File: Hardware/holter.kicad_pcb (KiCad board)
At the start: 2 copper layers, 33.5 x 48 mm, 270 parts, among them CN1 2TAP, CN2 2TAP, CN3 3TAP, IC1 256kx8, M1 USB_Power_Module, M2 USB_Power_Module, P1 CONN_01X07, P2 PROG, P3 SCREW, P4 BAT-, Q1 PMF170XP, Q2 PMF170XP, Q3 NTR4101PT1G, Q4 PMF170XP, Q5 PMF170XP, U1 TXB0106, U10 TS5A3159, U11 TS5A3159, U12 ESD_PROTECTOR, U13 ESD_PROTECTOR, U14 ESD_PROTECTOR, U15 ESD_PROTECTOR, U16 ESD_PROTECTOR, U17 ESD_PROTECTOR, U18 ESD_PROTECTOR, U19 ESD_PROTECTOR, U2 TXB0106, U20 ESD_PROTECTOR, U21 ESD_PROTECTOR, U22 ESD_PROTECTOR, U23 ESD_PROTECTOR, U24 TLV61220, U25 TLV61220, U26 TLV61220, U27 LM3671, U28 DS2710, U29 LIS2DH12, U3 TiWi-uB2, U4 STM32F4x1_64, U5 uSD, U6 ADS1298, U7 USBULC6-2M6, U8 USB2641, U9 OPA379, X1 32768, Y1 24 MHz, Y2 10 MHz

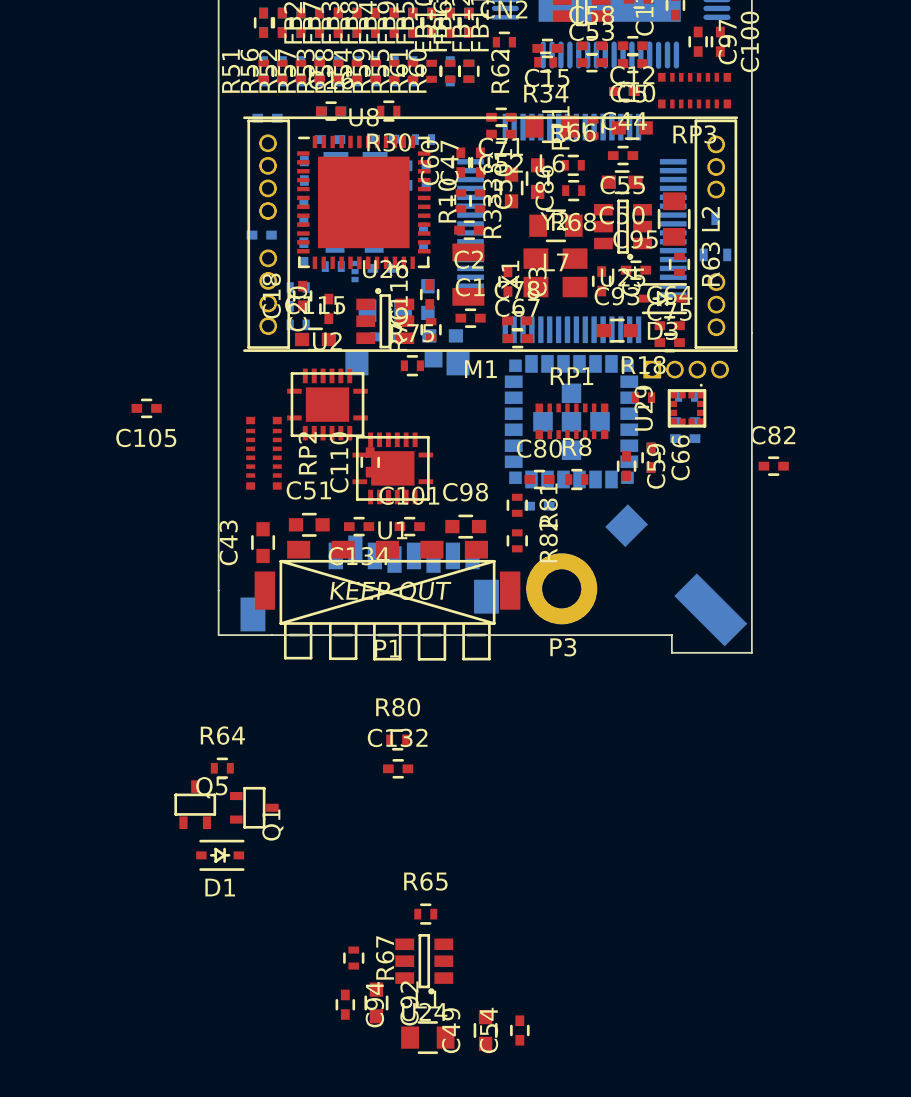
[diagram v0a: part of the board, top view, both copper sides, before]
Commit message: Placement + additional bypass capacitors.
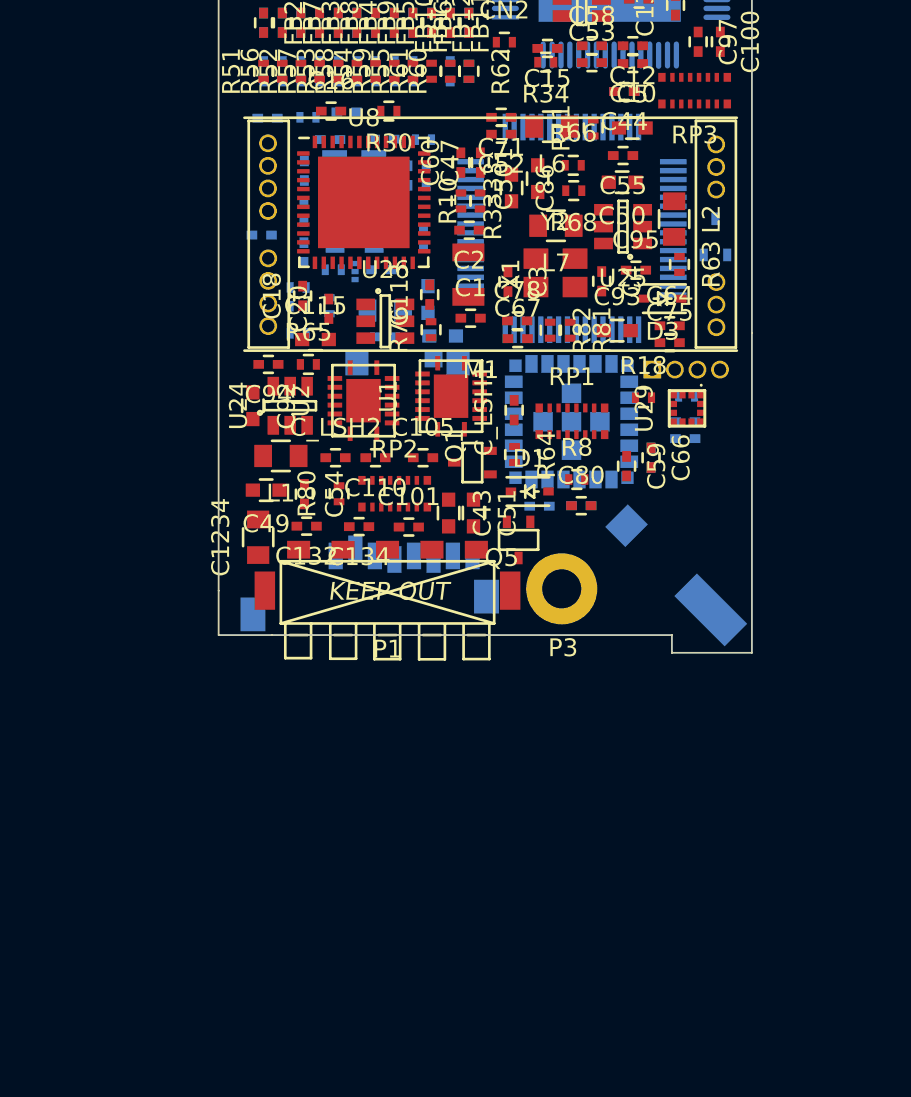
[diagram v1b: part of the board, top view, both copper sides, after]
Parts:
- removed C98: 10uF, Capacitors_SMD:C_0603
- added C1234: 22uF, Capacitors_SMD:C_0805, F.Cu at (77.2, 76.5)
- added C_LSH1: 100nF, Capacitors_SMD:C_0402, F.Cu at (91.6, 69.3)
- added C_LSH2: 100nF, Capacitors_SMD:C_0402, F.Cu at (81.6, 72.0)
- C51: value 10uF -> 22uF
- C82, R67, R75: moved to B.Cu
- moved C94 36.3 mm to (77.8, 66.8), turned to 180 degrees
- moved R67 35.3 mm to (79.5, 65.0), turned to 180 degrees
- moved C92 34.3 mm to (76.9, 69.1)
- moved L1 33.7 mm to (78.5, 71.9), turned to 180 degrees
- moved C49 32.8 mm to (77.7, 73.8), turned to 180 degrees
- moved C54 32.5 mm to (79.8, 74.1), turned to 270 degrees
- moved U24 32.1 mm to (79.0, 69.1), turned to 90 degrees
- moved R65 31.6 mm to (80.0, 66.8)
- moved D1 26.9 mm to (92.5, 73.9), turned to 0 degrees
- moved R64 24.1 mm to (91.7, 71.8), turned to 270 degrees
- moved Q5 23.5 mm to (91.9, 76.7), turned to 180 degrees
- moved Q1 23.0 mm to (89.3, 72.3), turned to 90 degrees
- moved C105 15.8 mm to (86.5, 72.0), turned to 0 degrees
- moved C132 14.6 mm to (80.0, 75.9), turned to 180 degrees
- moved R80 14.2 mm to (81.8, 74.0), turned to 90 degrees
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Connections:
- U1 pad 1: SDIO_D0 -> SDIO_CLK
- U1 pad 10: Net-(RP2-Pad6) -> Net-(RP2-Pad1)
- U1 pad 11: Net-(RP2-Pad5) -> Net-(RP2-Pad2)
- U1 pad 12: Net-(RP2-Pad4) -> Net-(RP2-Pad3)
- U1 pad 13: Net-(RP2-Pad3) -> Net-(RP2-Pad4)
- U1 pad 14: Net-(RP2-Pad2) -> Net-(RP2-Pad5)
- U1 pad 16: Net-(RP2-Pad1) -> Net-(RP2-Pad6)
- U1 pad 3: SDIO_D1 -> SDIO_CMD
- U1 pad 4: SDIO_D2 -> SDIO_D3
- U1 pad 5: SDIO_D3 -> SDIO_D2
- U1 pad 6: SDIO_CMD -> SDIO_D1
- U1 pad 7: SDIO_CLK -> SDIO_D0

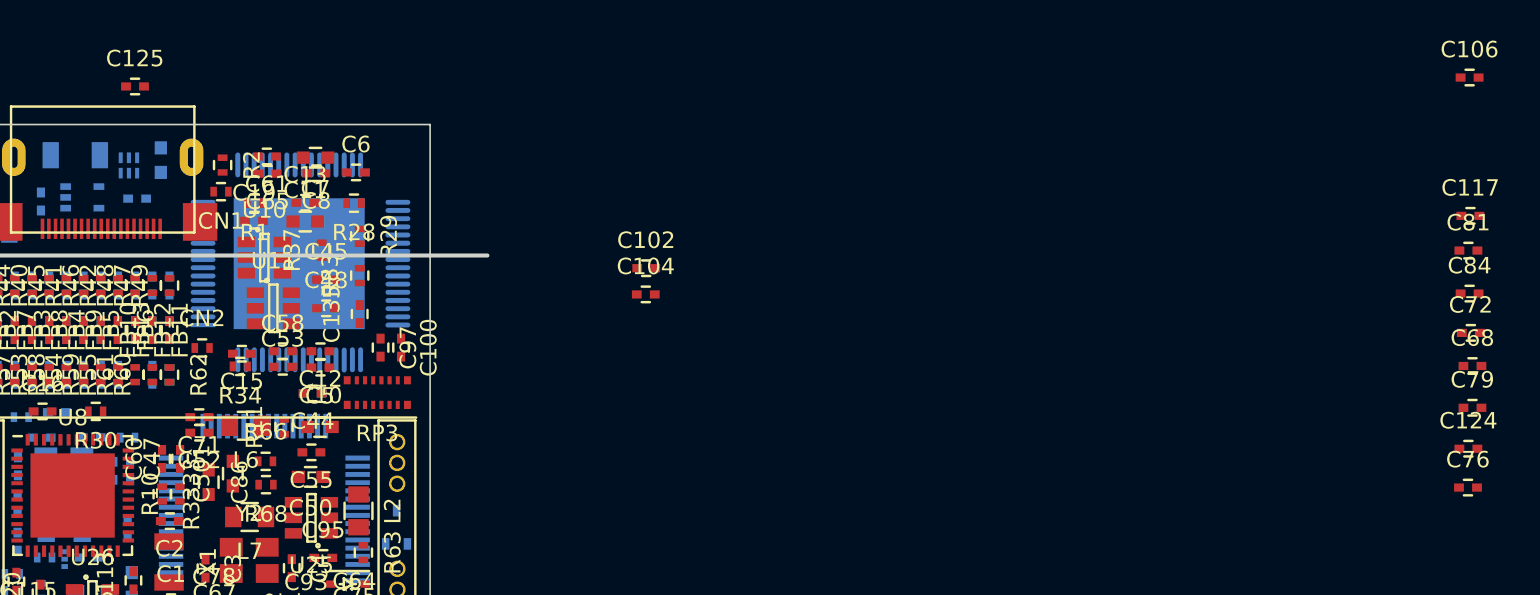
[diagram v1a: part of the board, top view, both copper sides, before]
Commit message: Removed unnecessary bypass capacitors.
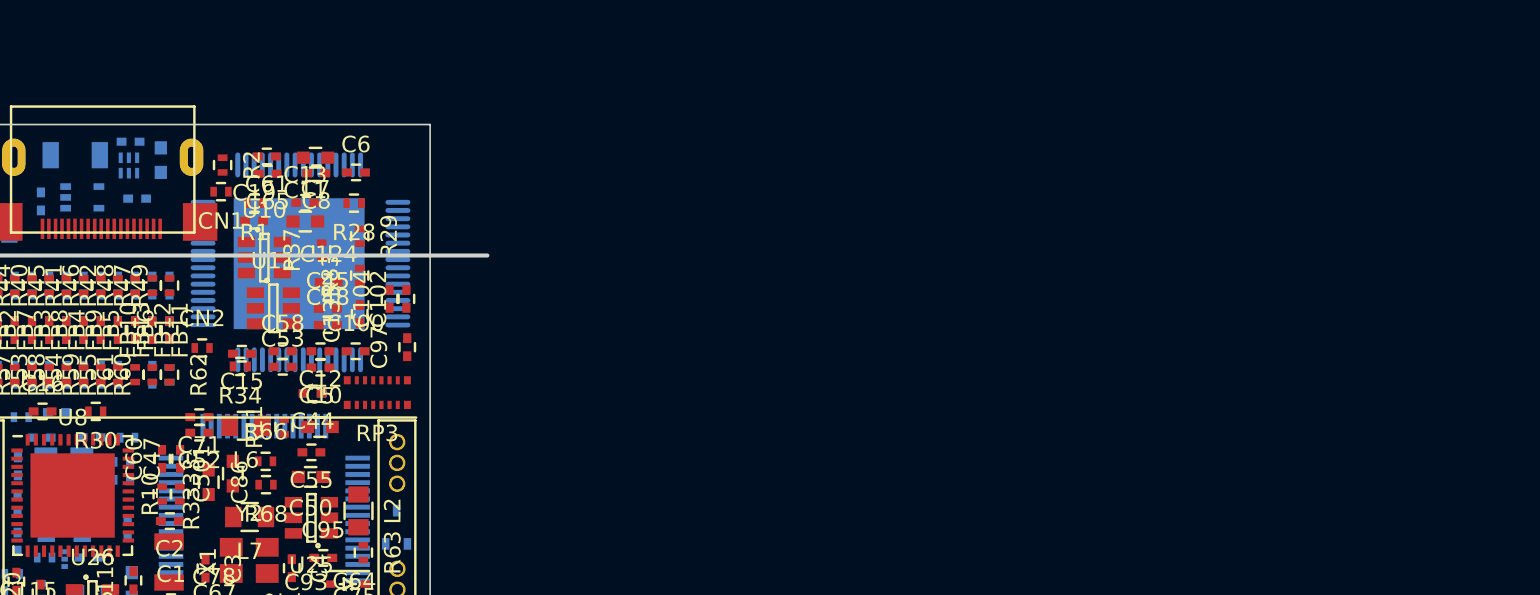
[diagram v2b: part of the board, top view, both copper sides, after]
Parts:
- removed C106, C68, C76, C81: 1uF, Capacitors_SMD:C_0402
- removed C117, C72, C79, C84: 100nF, Capacitors_SMD:C_0402
- C125: moved to B.Cu
- moved C124 70.4 mm to (98.8, 44.6)
- moved C104 15.7 mm to (102.5, 45.6), turned to 90 degrees
- moved C102 14.8 mm to (103.5, 45.6), turned to 90 degrees
- moved C125 3.39 mm to (86.7, 36.0), turned to 180 degrees
- moved C100 2.78 mm to (100.5, 48.9), turned to 0 degrees
- moved C45 1.78 mm to (98.8, 46.2)
- moved C97 1.63 mm to (103.6, 48.6), turned to 90 degrees
- moved C48 1.03 mm to (98.8, 47.2)

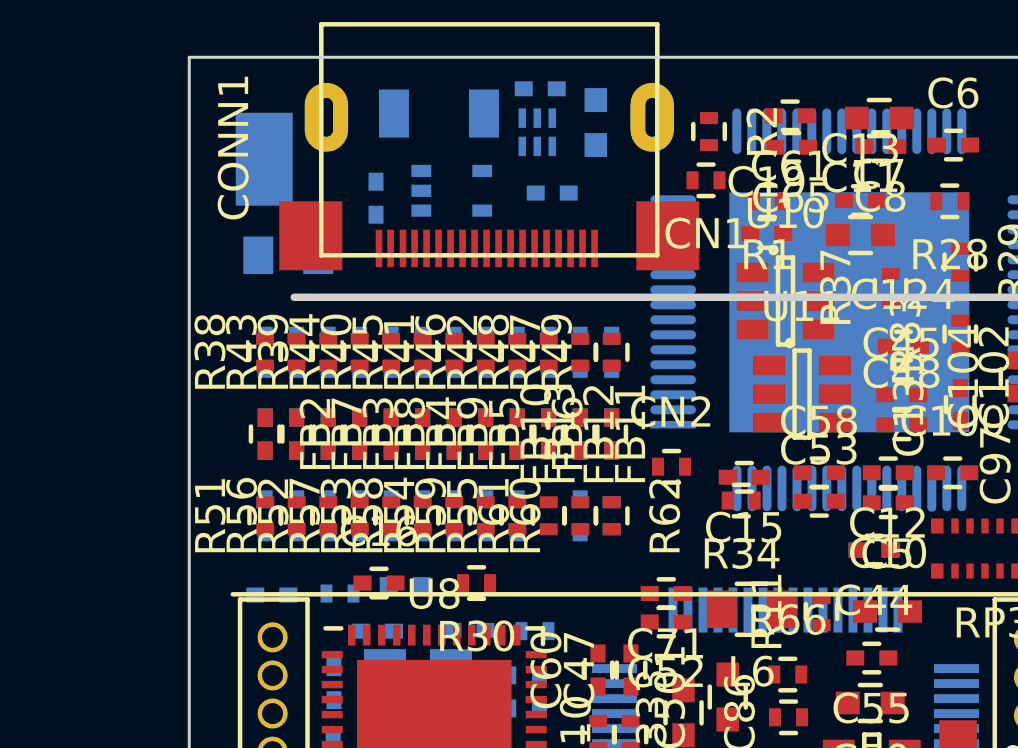
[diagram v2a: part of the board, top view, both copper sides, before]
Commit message: I/O filter connections on PCB.
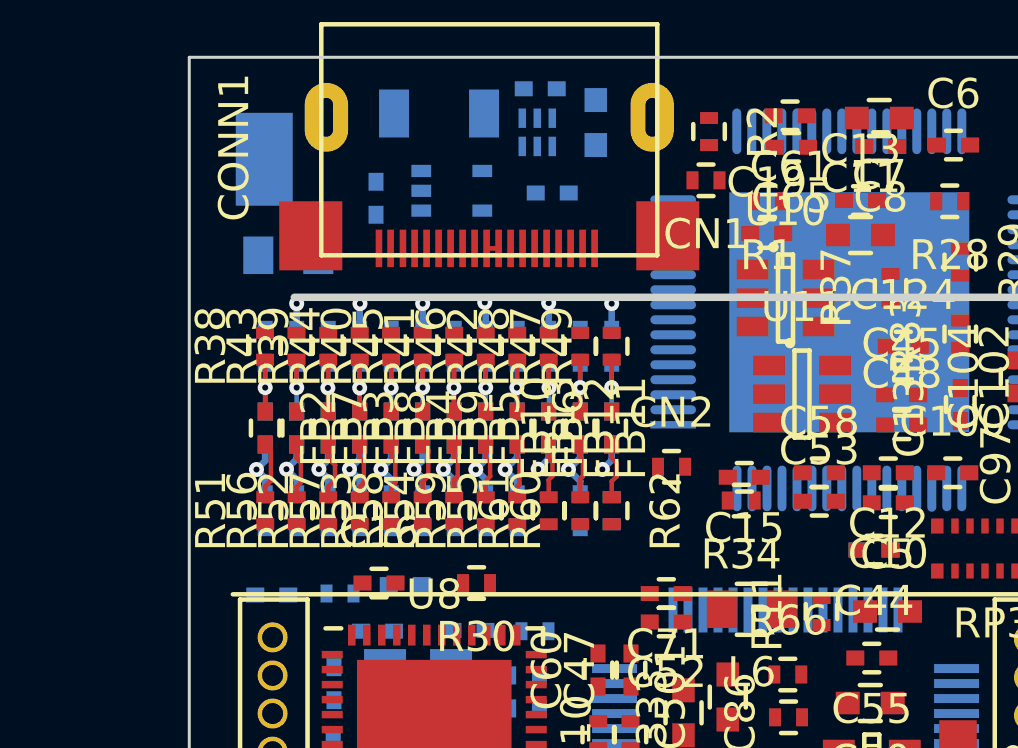
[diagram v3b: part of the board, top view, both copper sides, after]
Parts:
- moved C21 0.20 mm to (89.1, 47.4)
- moved C22 0.20 mm to (77.5, 47.4)
- moved C23 0.20 mm to (79.6, 47.4)
- moved C24 0.20 mm to (81.7, 47.4)
- moved C25 0.20 mm to (83.8, 47.4)
- moved C26 0.20 mm to (85.9, 47.4)
- moved C27 0.20 mm to (78.6, 47.4)
- moved C28 0.20 mm to (80.7, 47.4)
- moved C29 0.20 mm to (82.8, 47.4)
- moved C30 0.20 mm to (84.9, 47.4)
- moved C31 0.20 mm to (88.0, 47.4)
- moved C32 0.20 mm to (87.0, 47.4)
- moved FB10 0.20 mm to (84.9, 47.4)
- moved FB11 0.20 mm to (88.0, 47.4)
- moved FB12 0.20 mm to (87.0, 47.4)
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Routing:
- net GND: track 0.00 -> 26.6 mm, vias 0 -> 18
- net Net-(C26-Pad1): track 0.00 -> 3.37 mm, vias 0 -> 1
- net Net-(C25-Pad1): track 0.00 -> 3.37 mm, vias 0 -> 1
- net Net-(C23-Pad1): track 0.00 -> 3.37 mm, vias 0 -> 1
- net Net-(C22-Pad1): track 0.00 -> 3.35 mm, vias 0 -> 1
- net Net-(C31-Pad1): track 0.00 -> 3.35 mm, vias 0 -> 1
- net Net-(C28-Pad1): track 0.00 -> 3.35 mm, vias 0 -> 1
- net Net-(C32-Pad1): track 0.00 -> 2.56 mm, vias 0 -> 1
- net Net-(C24-Pad1): track 0.00 -> 2.56 mm, vias 0 -> 1
- net Net-(C27-Pad1): track 0.00 -> 2.55 mm, vias 0 -> 1
- net Net-(C30-Pad1): track 0.00 -> 2.55 mm, vias 0 -> 1
- net Net-(C29-Pad1): track 0.00 -> 2.55 mm, vias 0 -> 1
- net Net-(C21-Pad1): track 0.00 -> 2.55 mm, vias 0 -> 1
- net Net-(FB3-Pad2): track 0.00 -> 1.95 mm
- net Net-(FB9-Pad2): track 0.00 -> 1.91 mm
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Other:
- copper layers 2 -> 6
- net class Default: clearance 0.15 -> 0.1524; trace_width 0.15 -> 0.1524; via_dia 0.4 -> 0.5; via_drill 0.15 -> 0.2
- net class High Current added: clearance 0.1524, trace_width 1.5, via_dia 0.7, via_drill 0.4
- net class Power added: clearance 0.1524, trace_width 0.22, via_dia 0.5, via_drill 0.2
- rule trace_clearance: 0.15 -> 0.1524

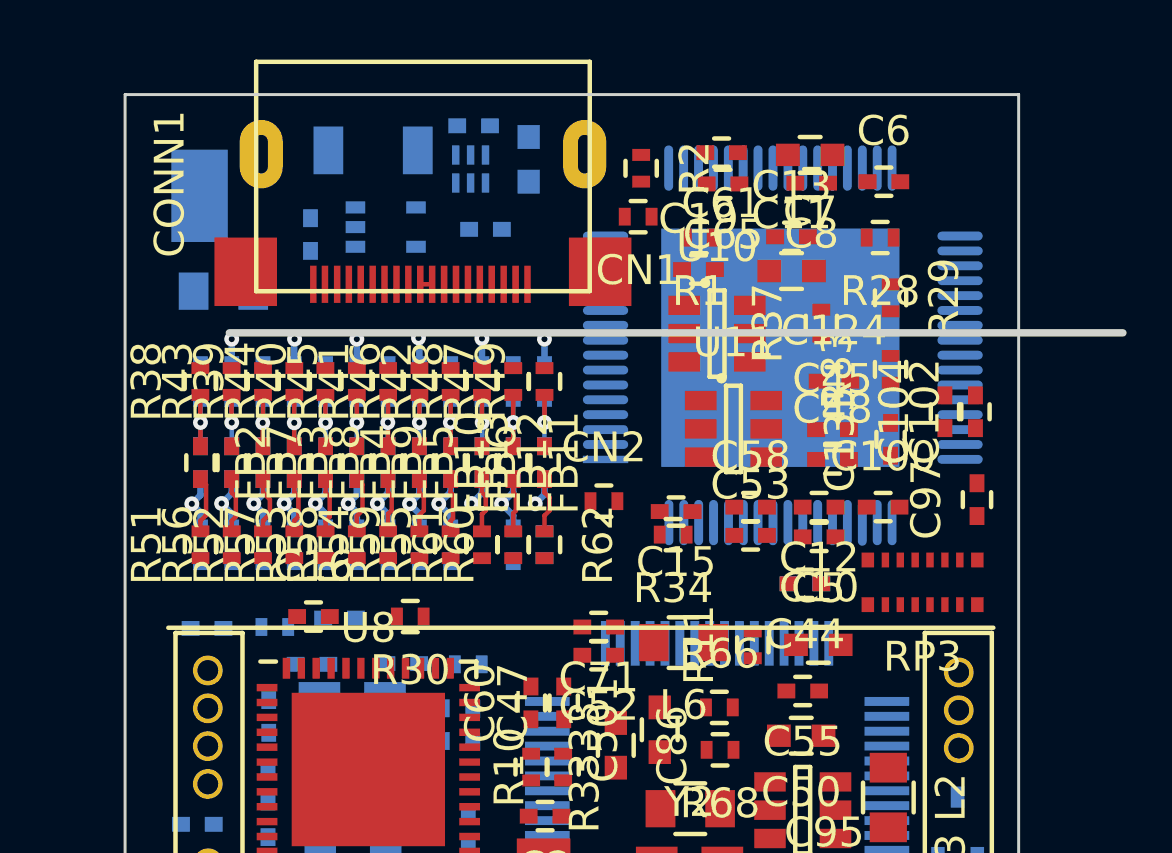
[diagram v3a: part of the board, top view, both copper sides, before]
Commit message: Fixed ADS1298 footprint. Routing of the analog parts.
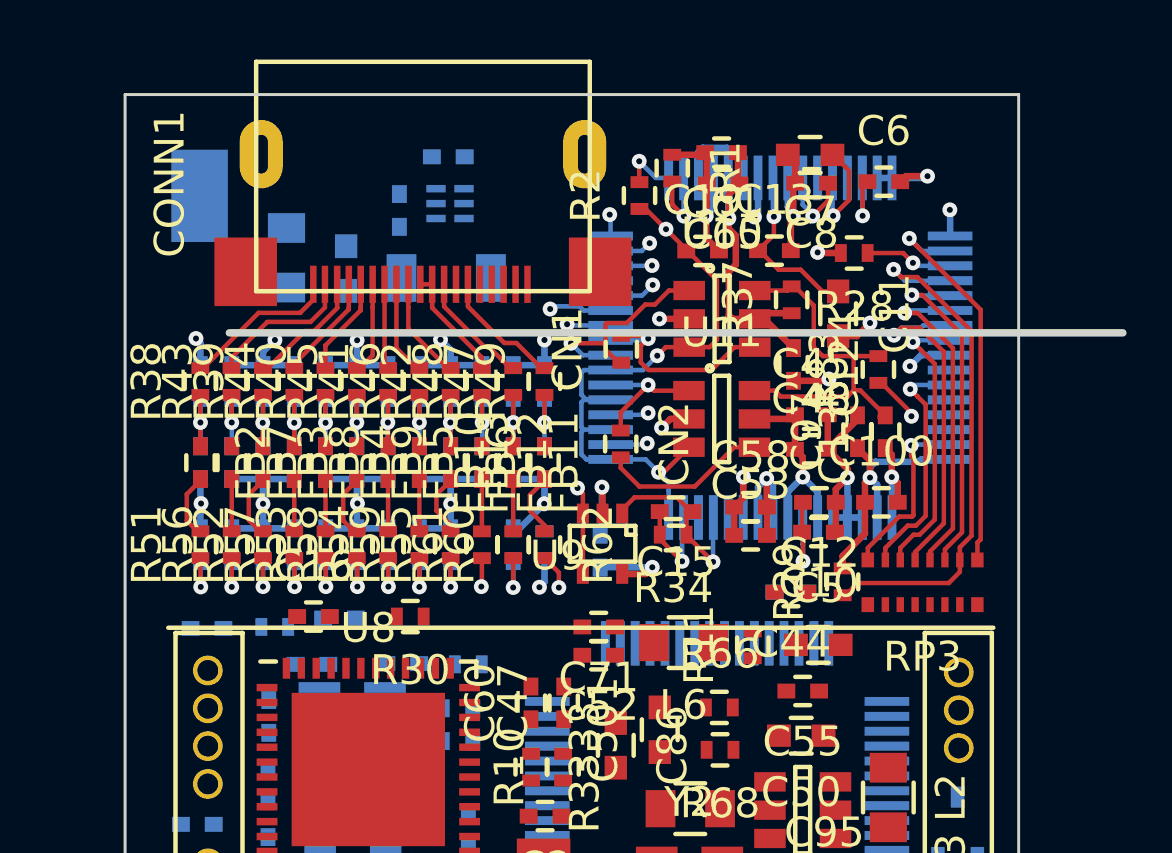
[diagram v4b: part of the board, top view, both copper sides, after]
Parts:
- removed C102: 1uF, Capacitors_SMD:C_0402
- removed C104: 100nF, Capacitors_SMD:C_0402
- U6: footprint Footprints:HTQFP_64 -> Housings_QFP:TQFP-64_10x10mm_Pitch0.5mm
- U9: moved to F.Cu
- moved C109 14.4 mm to (91.0, 50.3)
- moved U9 12.9 mm to (91.0, 50.1), turned to 180 degrees
- moved R29 9.67 mm to (99.1, 51.4), turned to 90 degrees
- moved FB1 7.14 mm to (82.4, 40.8), turned to 90 degrees
- moved F1 4.94 mm to (85.8, 41.2), turned to 180 degrees
- moved C97 4.61 mm to (99.6, 46.3)
- moved CN1 4.49 mm to (91.7, 43.5), turned to 90 degrees
- moved C137 2.96 mm to (84.2, 38.9), turned to 270 degrees
- moved R1 2.50 mm to (93.4, 37.5), turned to 270 degrees
- moved Rsense1 2.40 mm to (80.4, 40.5), turned to 270 degrees
- moved C11 2.12 mm to (98.9, 42.4), turned to 270 degrees
- moved CN2 2.00 mm to (91.6, 46.7), turned to 270 degrees
- moved C124 1.47 mm to (97.4, 44.1), turned to 270 degrees
- moved U7 1.35 mm to (85.9, 38.7), turned to 270 degrees
- moved C125 1.34 mm to (85.8, 37.1), turned to 0 degrees
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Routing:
- net GND: track 26.6 -> 75.1 mm, vias 18 -> 25
- net +2.8VA: track 0.00 -> 27.6 mm, vias 0 -> 4
- net Net-(C19-Pad1): track 0.00 -> 22.4 mm, vias 0 -> 3
- net Net-(R29-Pad1): track 0.00 -> 18.1 mm, vias 0 -> 1
- net Net-(RP3-Pad9): track 0.00 -> 13.4 mm, vias 0 -> 1
- net Net-(C135-Pad2): track 0.00 -> 12.3 mm
- net Net-(RP3-Pad13): track 0.00 -> 11.5 mm, vias 0 -> 1
- net Net-(RP3-Pad11): track 0.00 -> 11.3 mm, vias 0 -> 1
- net Net-(RP3-Pad12): track 0.00 -> 11.1 mm, vias 0 -> 1
- net +1V8: track 0.00 -> 10.2 mm, vias 0 -> 2
- net Net-(RP3-Pad14): track 0.00 -> 9.50 mm, vias 0 -> 1
- net V3_F: track 0.00 -> 9.32 mm, vias 0 -> 2
- net Net-(RP3-Pad15): track 0.00 -> 8.07 mm, vias 0 -> 1
- net Net-(CN1-Pad2): track 0.00 -> 7.38 mm, vias 0 -> 1
- net Net-(CN2-Pad2): track 0.00 -> 7.07 mm, vias 0 -> 1
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- added copper zone on Ground, net GND
